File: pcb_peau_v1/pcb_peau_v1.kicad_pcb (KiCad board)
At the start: 2 copper layers, 79.5 x 79.5 mm, 27 parts, among them J1 Conn_01x05, J2 Conn_01x05, J3 Conn_01x02, J4 Conn_02x08_Top_Bottom, J5 Conn_02x12_Top_Bottom, U2 TLC274, U3 CD74HC4067SM, U4 CD74HC4067SM, U5 CD74HC4067SM, U6 CD74HC4067SM, U7 TLC274, U8 TLC274, U9 TLC274

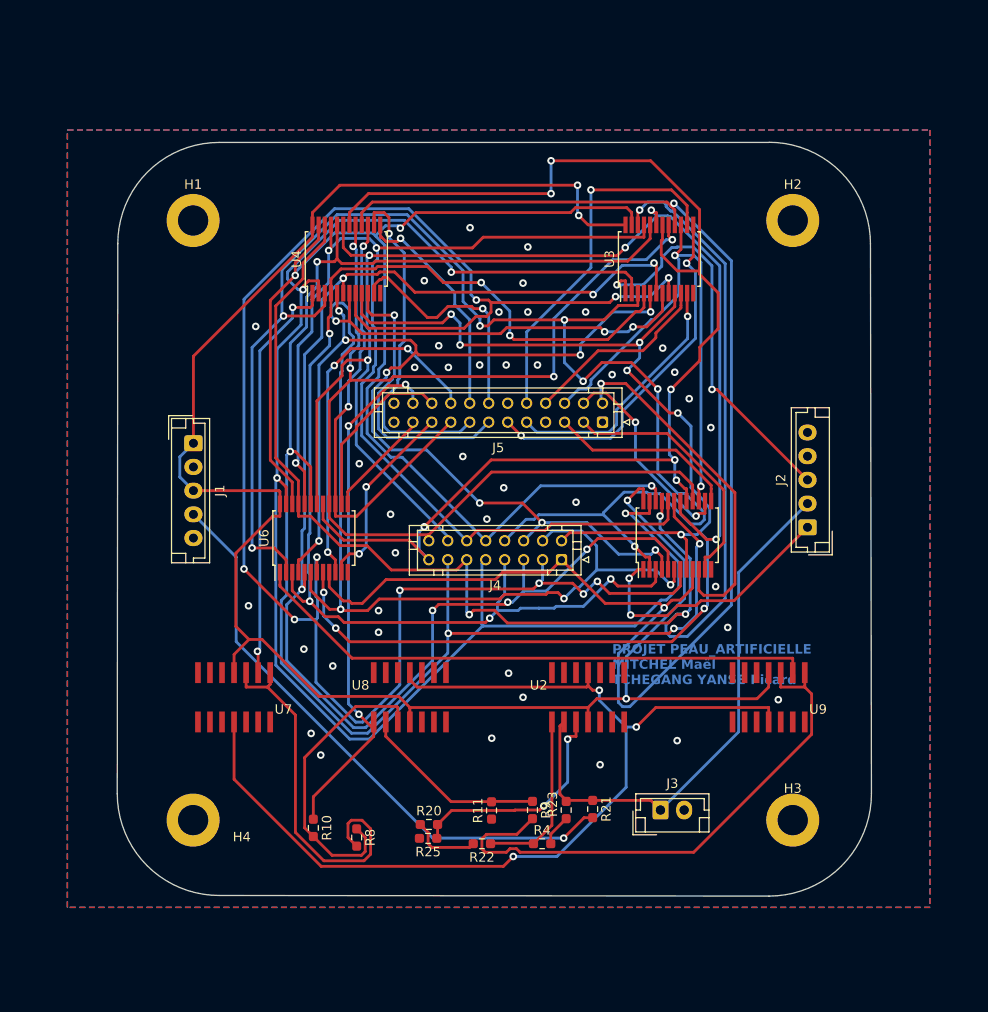
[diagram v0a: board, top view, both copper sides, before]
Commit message: Optimisation du cuivre
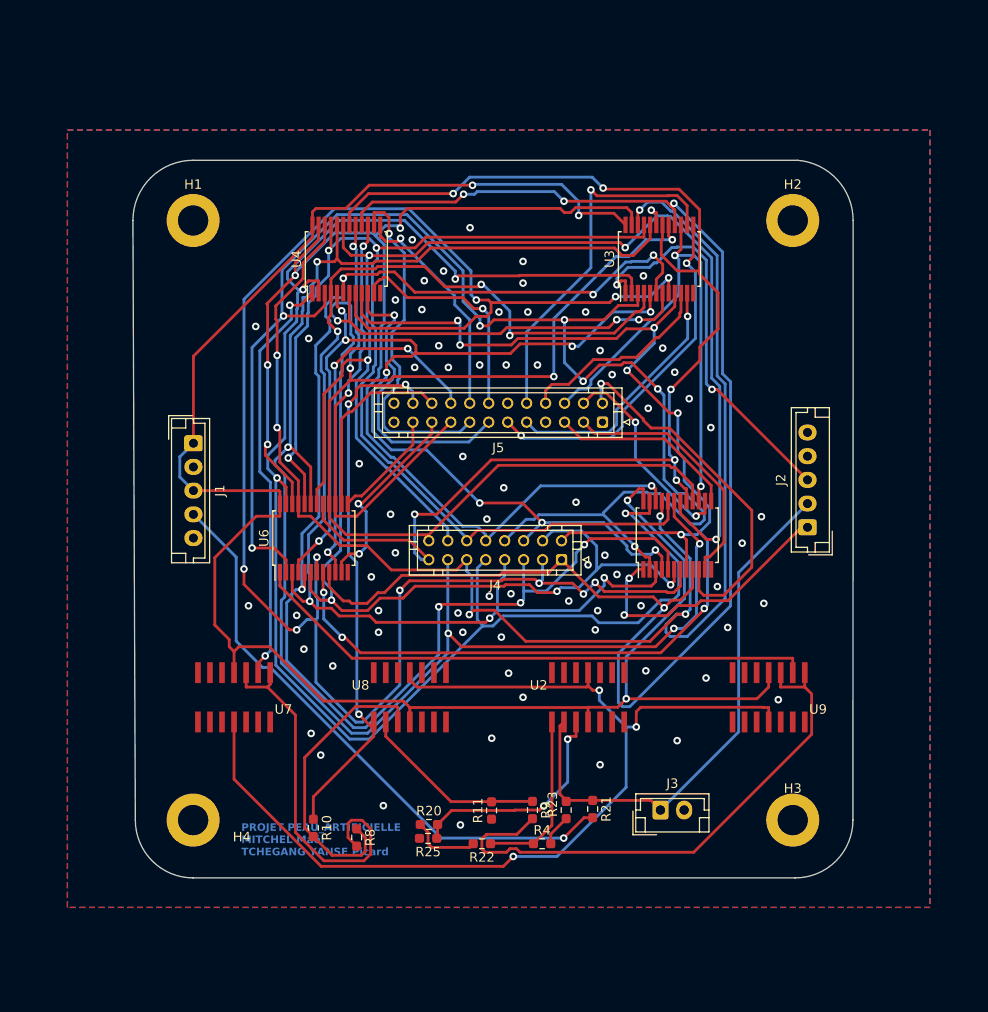
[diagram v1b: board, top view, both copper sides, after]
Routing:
- net Net-(J4-Pin_5): track 145.3 -> 149.5 mm
- net Net-(J4-Pin_13): track 166.5 -> 169.8 mm
- net Net-(J4-Pin_2): track 141.9 -> 144.7 mm
- net Net-(J4-Pin_9): track 167.0 -> 169.7 mm
- net +5V: track 198.0 -> 200.4 mm
- net Net-(J4-Pin_3): track 187.5 -> 189.5 mm
- net Net-(J4-Pin_10): track 134.1 -> 136.0 mm, vias 3 -> 5
- net Net-(J4-Pin_11): track 158.3 -> 160.1 mm, vias 4 -> 6
- net TRIOAOP1: track 56.1 -> 57.9 mm
- net A1: track 37.4 -> 38.9 mm
- net C2: track 18.6 -> 20.1 mm
- net Net-(J4-Pin_7): track 127.4 -> 128.8 mm
- net Net-(J4-Pin_15): track 135.4 -> 134.2 mm
- net A4: track 30.2 -> 31.3 mm
- net Net-(J4-Pin_12): track 128.1 -> 129.1 mm
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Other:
- board size 79.5 x 79.5 mm -> 76 x 75.7 mm

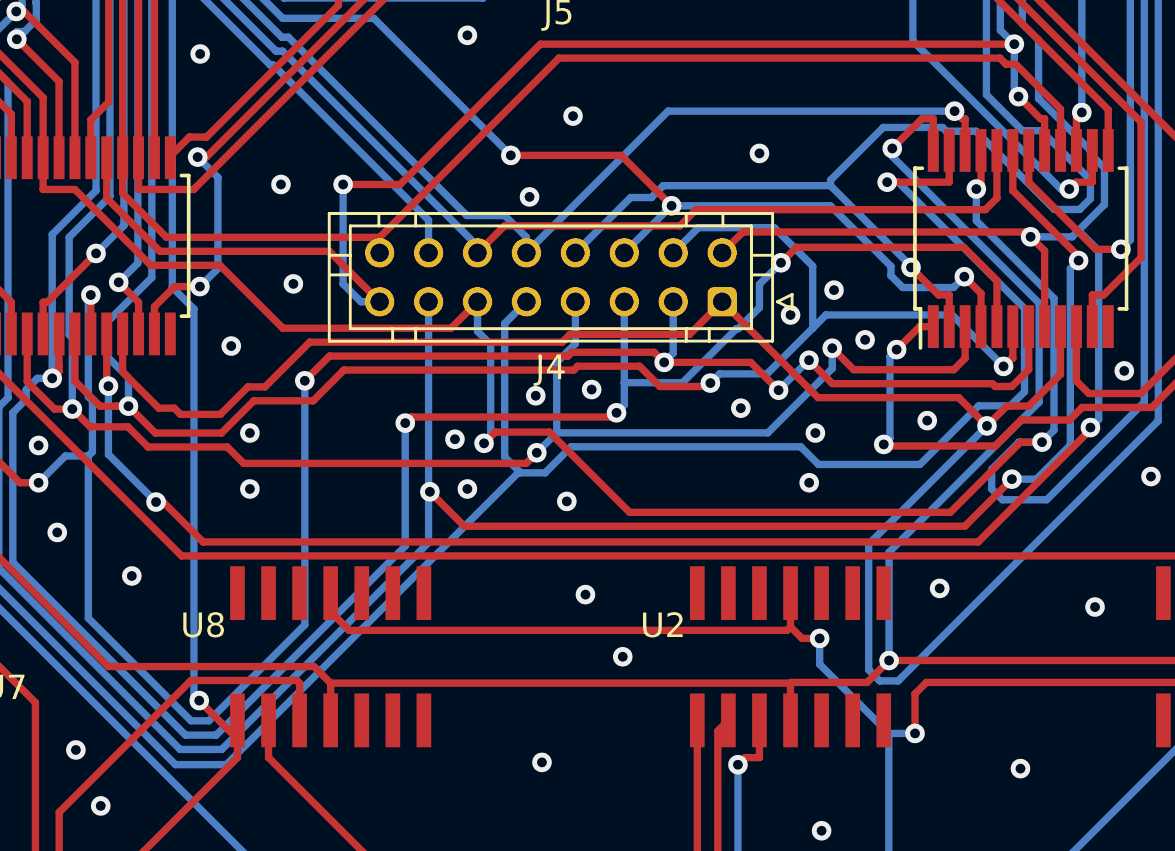
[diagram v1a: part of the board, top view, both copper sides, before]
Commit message: Génération des drills / gerbers
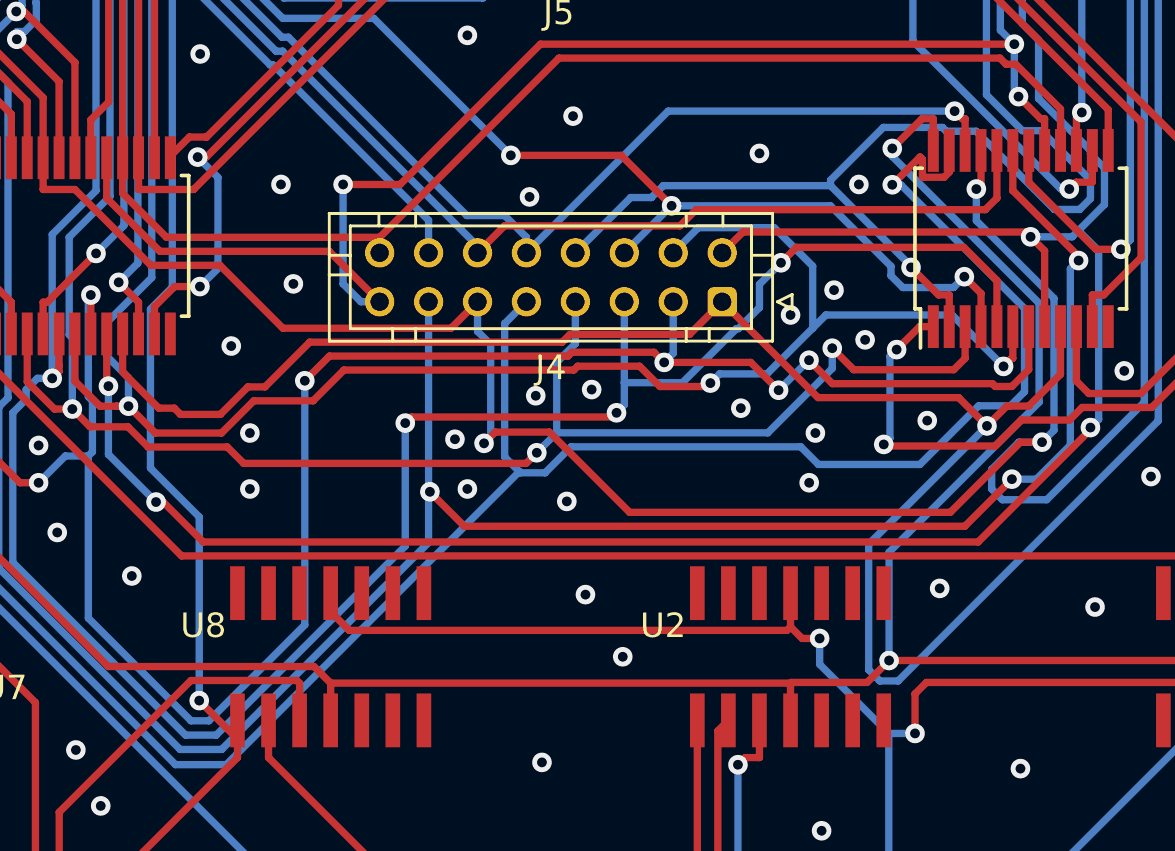
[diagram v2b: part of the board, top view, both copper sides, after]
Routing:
- net TRIOAOP1: track 57.9 -> 58.6 mm
- net 0: vias 70 -> 71
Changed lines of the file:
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@@
       (drillshape 0)
       (scaleselection 1)
-      (outputdirectory "PCB BIS peau artificielle MITCHEL YANSE/")
+      (outputdirectory "PCB Optimisé MITCHEL YANSE/")
     )
   )
@@
   (via (at 204.47 51.308) (size 0.8) (drill 0.4) (layers "F.Cu" "B.Cu") (free) (net 1))
   (via (at 186.182 92.202) (size 0.8) (drill 0.4) (layers "F.Cu" "B.Cu") (free) (net 1))
+  (via (at 219.71 81.534) (size 0.8) (drill 0.4) (layers "F.Cu" "B.Cu") (free) (net 1))
   (via (at 181.102 91.186) (size 0.8) (drill 0.4) (layers "F.Cu" "B.Cu") (free) (net 1))
   (via (at 236.982 101.092) (size 0.8) (drill 0.4) (layers "F.Cu" "B.Cu") (free) (net 1))
@@
   (segment (start 218.5516 81.5828) (end 211.7149 81.5828) (width 0.3) (layer "B.Cu") (net 16))
   (segment (start 211.7149 81.5828) (end 211.23 82.0677) (width 0.3) (layer "B.Cu") (net 16))
+  (segment (start 223.402 81.034) (end 223.402 80.144) (width 0.3) (layer "F.Cu") (net 17))
   (segment (start 185.067 78.6583) (end 184.1121 77.7034) (width 0.3) (layer "F.Cu") (net 17))
-  (segment (start 223.402 80.144) (end 223.402 81.4409) (width 0.3) (layer "F.Cu") (net 17))
   (segment (start 187.4299 56.9132) (end 187.4299 56.9131) (width 0.3) (layer "F.Cu") (net 17))
   (segment (start 221.1764 56.33) (end 221.517 56.6706) (width 0.3) (layer "F.Cu") (net 17))
   (segment (start 209.718344 56.33) (end 221.1764 56.33) (width 0.3) (layer "F.Cu") (net 17))
-  (segment (start 223.402 81.4409) (end 220.8669 81.4409) (width 0.3) (layer "F.Cu") (net 17))
+  (segment (start 222.307 81.239) (end 223.197 81.239) (width 0.3) (layer "F.Cu") (net 17))
+  (segment (start 221.074001 81.54655) (end 222.211225 80.409326) (width 0.3) (layer "F.Cu") (net 17))
   (segment (start 203.2471 56.388) (end 209.660344 56.388) (width 0.3) (layer "F.Cu") (net 17))
   (segment (start 221.517 56.6706) (end 221.517 58.21) (width 0.3) (layer "F.Cu") (net 17))
   (segment (start 186.8537 57.4894) (end 187.4299 56.9132) (width 0.3) (layer "F.Cu") (net 17))
   (segment (start 185.067 80.442) (end 185.067 78.6583) (width 0.3) (layer "F.Cu") (net 17))
+  (segment (start 223.197 81.239) (end 223.402 81.034) (width 0.3) (layer "F.Cu") (net 17))
   (segment (start 188.497 58.21) (end 188.497 56.9131) (width 0.3) (layer "F.Cu") (net 17))
   (segment (start 209.660344 56.388) (end 209.718344 56.33) (width 0.3) (layer "F.Cu") (net 17))
+  (segment (start 222.211225 80.409326) (end 222.307 80.505101) (width 0.3) (layer "F.Cu") (net 17))
   (segment (start 187.4299 56.9131) (end 188.497 56.9131) (width 0.3) (layer "F.Cu") (net 17))
+  (segment (start 222.307 80.505101) (end 222.307 81.239) (width 0.3) (layer "F.Cu") (net 17))
   (segment (start 202.9126 56.7225) (end 203.2471 56.388) (width 0.3) (layer "F.Cu") (net 17))
   (segment (start 186.8537 57.8432) (end 186.8537 57.4894) (width 0.3) (layer "F.Cu") (net 17))
   (via (at 202.9126 56.7225) (size 0.8) (drill 0.4) (layers "F.Cu" "B.Cu") (net 17))
   (via (at 184.1121 77.7034) (size 0.8) (drill 0.4) (layers "F.Cu" "B.Cu") (net 17))
-  (via (at 220.8669 81.4409) (size 0.8) (drill 0.4) (layers "F.Cu" "B.Cu") (net 17))
+  (via (at 221.074001 81.54655) (size 0.8) (drill 0.4) (layers "F.Cu" "B.Cu") (net 17))
   (via (at 186.8537 57.8432) (size 0.8) (drill 0.4) (layers "F.Cu" "B.Cu") (net 17))
-  (segment (start 224.6046 90.5804) (end 225.9036 90.5804) (width 0.3) (layer "B.Cu") (net 17))
   (segment (start 184.1121 77.7034) (end 183.9846 77.8309) (width 0.3) (layer "B.Cu") (net 17))
   (segment (start 193.8537 105.2477) (end 205.8306 93.2708) (width 0.3) (layer "B.Cu") (net 17))
   (segment (start 185.2127 55.9917) (end 185.2127 56.7191) (width 0.3) (layer "B.Cu") (net 17))
   (segment (start 202.9126 56.7225) (end 202.9126 55.8908) (width 0.3) (layer "B.Cu") (net 17))
-  (segment (start 207.948456 92.2557) (end 217.334044 92.2557) (width 0.3) (layer "B.Cu") (net 17))
   (segment (start 185.2127 56.7191) (end 186.3368 57.8432) (width 0.3) (layer "B.Cu") (net 17))
+  (segment (start 226.4809 86.6032) (end 226.4809 90.0031) (width 0.3) (layer "B.Cu") (net 17))
   (segment (start 186.3368 57.8432) (end 186.6505 57.8432) (width 0.3) (layer "B.Cu") (net 17))
   (segment (start 205.232 87.218) (end 205.232 92.6722) (width 0.3) (layer "B.Cu") (net 17))
-  (segment (start 205.8306 93.2708) (end 205.8799 93.3201) (width 0.3) (layer "B.Cu") (net 17))
+  (segment (start 217.334044 92.2557) (end 207.948456 92.2557) (width 0.3) (layer "B.Cu") (net 17))
   (segment (start 191.7771 105.2477) (end 193.8537 105.2477) (width 0.3) (layer "B.Cu") (net 17))
-  (segment (start 221.3186 81.4409) (end 220.8669 81.4409) (width 0.3) (layer "B.Cu") (net 17))
+  (segment (start 221.074001 81.54655) (end 221.42425 81.54655) (width 0.3) (layer "B.Cu") (net 17))
+  (segment (start 206.884056 93.3201) (end 205.8799 93.3201) (width 0.3) (layer "B.Cu") (net 17))
   (segment (start 206.122 86.328) (end 205.232 87.218) (width 0.3) (layer "B.Cu") (net 17))
   (segment (start 184.936 62.450402) (end 184.936 73.507656) (width 0.3) (layer "B.Cu") (net 17))
-  (segment (start 206.884056 93.3201) (end 207.948456 92.2557) (width 0.3) (layer "B.Cu") (net 17))
   (segment (start 186.6505 57.8432) (end 186.8537 57.8432) (width 0.3) (layer "B.Cu") (net 17))
   (segment (start 197.5525 50.5307) (end 190.6737 50.5307) (width 0.3) (layer "B.Cu") (net 17))
-  (segment (start 217.334044 92.2557) (end 218.056944 92.9786) (width 0.3) (layer "B.Cu") (net 17))
-  (segment (start 218.056944 92.9786) (end 222.2064 92.9786) (width 0.3) (layer "B.Cu") (net 17))
+  (segment (start 226.4809 90.0031) (end 225.9036 90.5804) (width 0.3) (layer "B.Cu") (net 17))
   (segment (start 183.9846 77.8309) (end 183.9846 97.4552) (width 0.3) (layer "B.Cu") (net 17))
   (segment (start 190.6737 50.5307) (end 185.2127 55.9917) (width 0.3) (layer "B.Cu") (net 17))
+  (segment (start 218.056944 92.9786) (end 217.334044 92.2557) (width 0.3) (layer "B.Cu") (net 17))
   (segment (start 186.1873 61.199102) (end 184.936 62.450402) (width 0.3) (layer "B.Cu") (net 17))
+  (segment (start 221.42425 81.54655) (end 226.4809 86.6032) (width 0.3) (layer "B.Cu") (net 17))
   (segment (start 186.2712 59.821331) (end 186.1873 59.905231) (width 0.3) (layer "B.Cu") (net 17))
-  (segment (start 225.9036 90.5804) (end 226.4809 90.0031) (width 0.3) (layer "B.Cu") (net 17))
   (segment (start 205.232 92.6722) (end 205.8306 93.2708) (width 0.3) (layer "B.Cu") (net 17))
   (segment (start 183.134 76.7253) (end 184.1121 77.7034) (width 0.3) (layer "B.Cu") (net 17))
-  (segment (start 226.4809 86.6032) (end 221.3186 81.4409) (width 0.3) (layer "B.Cu") (net 17))
   (segment (start 202.9126 55.8908) (end 197.5525 50.5307) (width 0.3) (layer "B.Cu") (net 17))
   (segment (start 186.2712 58.2225) (end 186.2712 59.821331) (width 0.3) (layer "B.Cu") (net 17))
   (segment (start 186.1873 59.905231) (end 186.1873 61.199102) (width 0.3) (layer "B.Cu") (net 17))
+  (segment (start 224.6046 90.5804) (end 222.2064 92.9786) (width 0.3) (layer "B.Cu") (net 17))
   (segment (start 183.9846 97.4552) (end 191.7771 105.2477) (width 0.3) (layer "B.Cu") (net 17))
-  (segment (start 226.4809 90.0031) (end 226.4809 86.6032) (width 0.3) (layer "B.Cu") (net 17))
-  (segment (start 205.8799 93.3201) (end 206.884056 93.3201) (width 0.3) (layer "B.Cu") (net 17))
+  (segment (start 207.948456 92.2557) (end 206.884056 93.3201) (width 0.3) (layer "B.Cu") (net 17))
+  (segment (start 225.9036 90.5804) (end 224.6046 90.5804) (width 0.3) (layer "B.Cu") (net 17))
   (segment (start 186.6505 57.8432) (end 186.2712 58.2225) (width 0.3) (layer "B.Cu") (net 17))
-  (segment (start 222.2064 92.9786) (end 224.6046 90.5804) (width 0.3) (layer "B.Cu") (net 17))
+  (segment (start 205.8799 93.3201) (end 205.8306 93.2708) (width 0.3) (layer "B.Cu") (net 17))
+  (segment (start 222.2064 92.9786) (end 218.056944 92.9786) (width 0.3) (layer "B.Cu") (net 17))
   (segment (start 183.134 75.309656) (end 183.134 76.7253) (width 0.3) (layer "B.Cu") (net 17))
   (segment (start 184.936 73.507656) (end 183.134 75.309656) (width 0.3) (layer "B.Cu") (net 17))
@@
   (via (at 192.7479 102.6298) (size 0.8) (drill 0.4) (layers "F.Cu" "B.Cu") (net 46))
   (via (at 191.6483 69.908498) (size 0.8) (drill 0.4) (layers "F.Cu" "B.Cu") (net 46))
-  (segment (start 192.532 102.4139) (end 192.7479 102.6298) (width 0.3) (layer "B.Cu") (net 46))
-  (segment (start 191.6459 85.737456) (end 192.532 86.623556) (width 0.3) (layer "B.Cu") (net 46))
+  (segment (start 190.754 86.629356) (end 190.754 93.126394) (width 0.3) (layer "B.Cu") (net 46))
+  (segment (start 191.6459 69.910898) (end 191.6459 85.737456) (width 0.3) (layer "B.Cu") (net 46))
+  (segment (start 191.6459 85.737456) (end 190.754 86.629356) (width 0.3) (layer "B.Cu") (net 46))
+  (segment (start 192.7479 95.120294) (end 192.7479 102.6298) (width 0.3) (layer "B.Cu") (net 46))
   (segment (start 191.6483 69.908498) (end 191.6459 69.910898) (width 0.3) (layer "B.Cu") (net 46))
-  (segment (start 192.532 86.623556) (end 192.532 102.4139) (width 0.3) (layer "B.Cu") (net 46))
+  (segment (start 190.754 93.126394) (end 192.7479 95.120294) (width 0.3) (layer "B.Cu") (net 46))
   (segment (start 197.6706 67.8411) (end 198.44 68.6105) (width 0.3) (layer "B.Cu") (net 46))
   (segment (start 198.44 68.6105) (end 198.44 69.818) (width 0.3) (layer "B.Cu") (net 46))
-  (segment (start 191.6459 69.910898) (end 191.6459 85.737456) (width 0.3) (layer "B.Cu") (net 46))
   (segment (start 211.1061 116.2346) (end 206.6839 116.2346) (width 0.3) (layer "F.Cu") (net 47))
   (segment (start 211.1575 116.286) (end 211.1061 116.2346) (width 0.3) (layer "F.Cu") (net 47))

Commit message: pdb bulletproof
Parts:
- moved H2 14.6 mm to (247.7, 39.1)
- moved H1 14.2 mm to (166.9, 39.1)
- moved H3 13.9 mm to (247.7, 124.2)
- moved H4 13.0 mm to (167.1, 124.0)
- moved J1 11.6 mm to (170.8, 63.4)
- moved J2 10.4 mm to (244.2, 73.4)
- moved U3 8.07 mm to (228.2, 47.5)
- moved U4 7.58 mm to (189.6, 47.3)
- moved U7 7.18 mm to (174.5, 105.9)
- moved U9 6.71 mm to (240.0, 106.2)
- moved J5 4.79 mm to (218.3, 67.0)
- moved U6 4.71 mm to (183.7, 86.1)
- moved U5 4.54 mm to (230.2, 86.1)
- moved U2 3.93 mm to (220.0, 103.3)
- moved J3 3.71 mm to (224.6, 116.4)
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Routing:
- net Net-(J4-Pin_2): track 144.7 -> 210.5 mm, vias 9 -> 6
- net +5V: track 200.4 -> 262.6 mm
- net Net-(J4-Pin_7): track 128.8 -> 185.0 mm, vias 6 -> 8
- net Net-(J4-Pin_12): track 129.1 -> 180.2 mm, vias 3 -> 5
- net Net-(J4-Pin_14): track 138.5 -> 183.3 mm, vias 5 -> 9
- net Net-(J4-Pin_6): track 121.6 -> 166.0 mm, vias 9 -> 8
- net Net-(J4-Pin_9): track 170.2 -> 130.1 mm, vias 4 -> 5
- net A1: track 38.9 -> 76.4 mm, vias 1 -> 2
- net Net-(J4-Pin_4): track 133.0 -> 160.6 mm
- net AOP0IN+: track 57.9 -> 84.3 mm
- net Net-(J4-Pin_15): track 134.2 -> 159.7 mm
- net -5V: track 107.1 -> 81.7 mm, vias 3 -> 4
- net NE2: track 48.7 -> 73.1 mm, vias 2 -> 5
- net AOP1: track 44.1 -> 67.3 mm
- net B3: track 27.2 -> 47.9 mm
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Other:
- board size 76 x 75.7 mm -> 93.2 x 97.3 mm

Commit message: ça marche pas
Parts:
- R10, R11, R20, R21, R22, R23, R25, R4, R8, R9: footprint Resistor_SMD:R_0603_1608Metric_Pad0.98x0.95mm_HandSolder -> Resistor_SMD:R_0805_2012Metric_Pad1.20x1.40mm_HandSolder
- moved R25 0.51 mm to (200.1, 119.9)
- moved R21 0.22 mm to (217.6, 116.3)
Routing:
- net Net-(R20-Pad1): track 7.25 -> 8.42 mm
- net Net-(U7A-+): track 29.9 -> 30.9 mm
- net +5V: track 262.6 -> 263.6 mm
- net 0: vias 73 -> 74
